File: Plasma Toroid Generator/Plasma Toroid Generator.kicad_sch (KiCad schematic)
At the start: 14 parts, among them J1 Conn_01x02, J2 Conn_01x01, J3 Conn_01x01, J4 Conn_01x01, J5 Conn_01x01, Q1 IRFP260

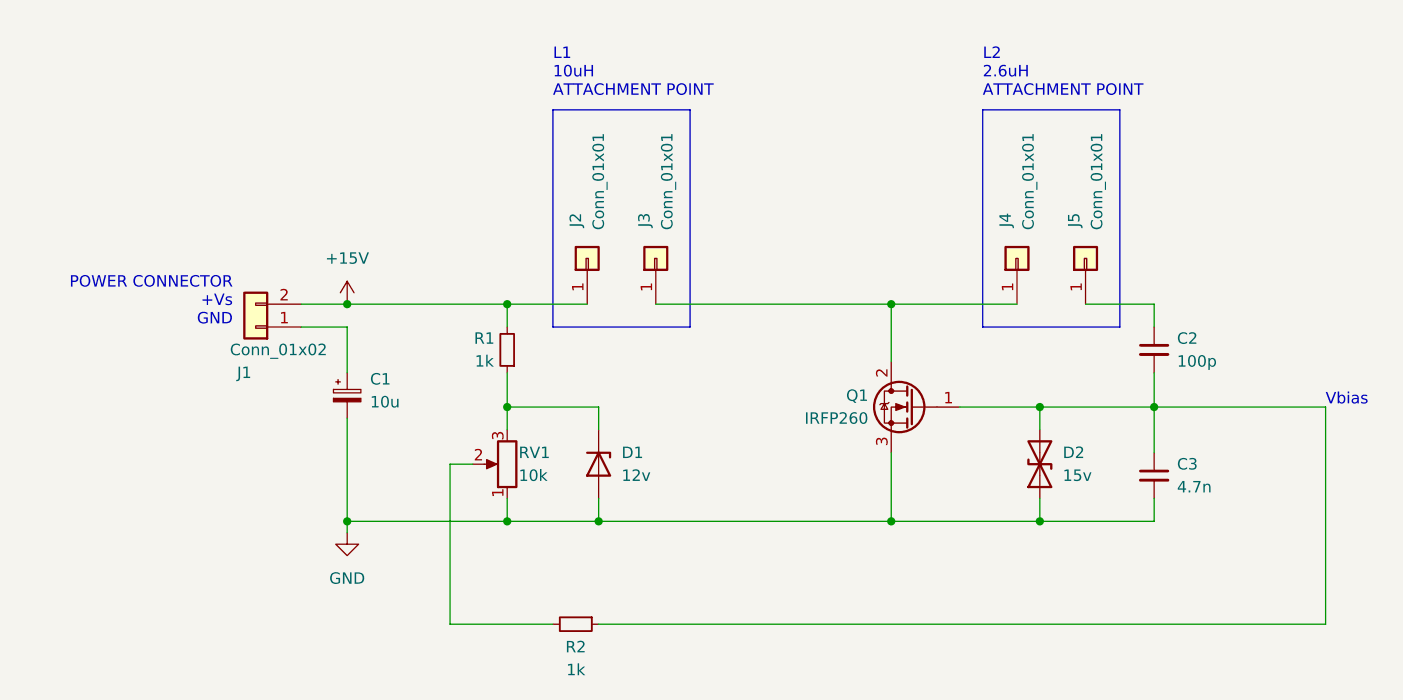
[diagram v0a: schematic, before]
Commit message: Updated PCB layout to fix errors in cap placement
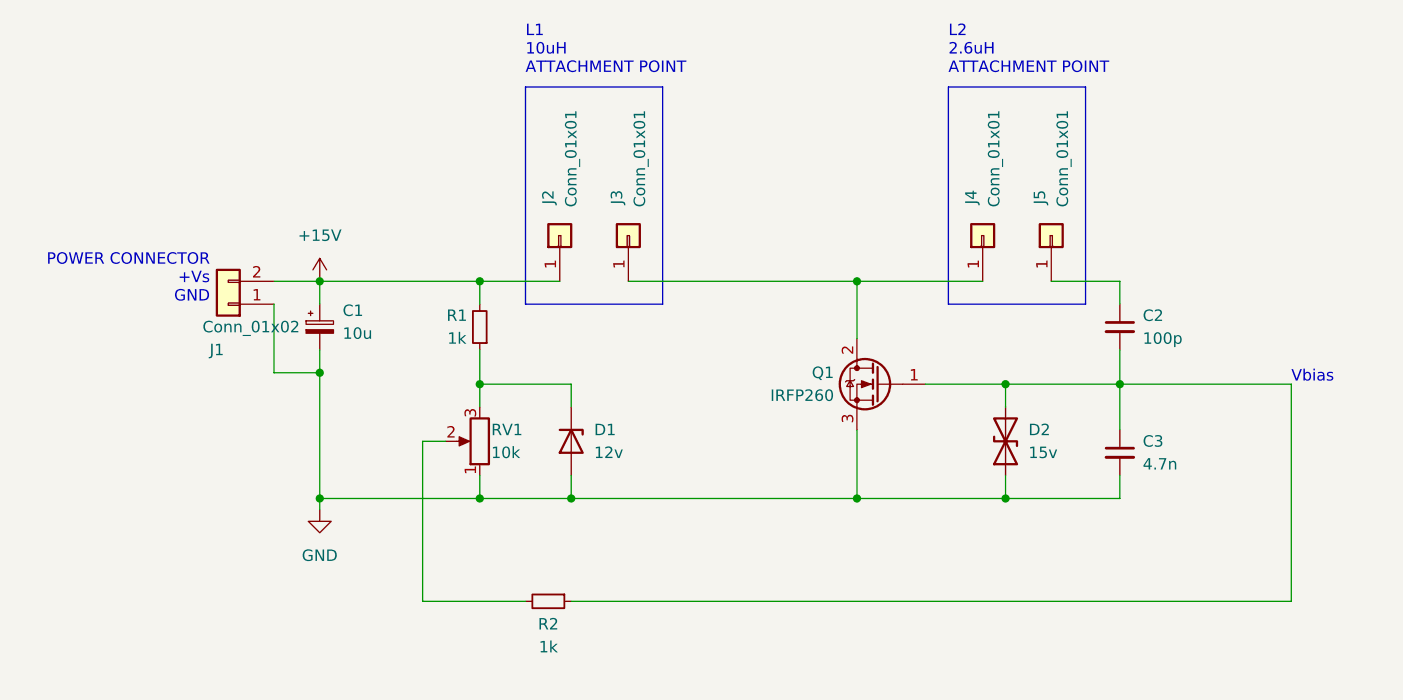
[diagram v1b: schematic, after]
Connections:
- net +15V: now also C1.1
- net GND: now also J1.1 (Pin_1)
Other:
- moved on the sheet: C1, C2, C3, D1, D2, J1, J2, J3, J4, J5, Q1, R1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

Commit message: Updates to model to accurately reflect the physical circuit
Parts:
- J1: footprint TerminalBlock_Phoenix:TerminalBlock_Phoenix_PT-1,5-2-3.5-H_1x02_P3.50mm_Horizontal -> TerminalBlock_Phoenix:TerminalBlock_Phoenix_PT-1,5-2-5.0-H_1x02_P5.00mm_Horizontal
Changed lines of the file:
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@@
     (property "Reference" "J1" (id 0) (at 80.01 91.44 0))
     (property "Value" "Conn_01x02" (id 1) (at 83.82 88.9 0))
-    (property "Footprint" "TerminalBlock_Phoenix:TerminalBlock_Phoenix_PT-1,5-2-3.5-H_1x02_P3.50mm_Horizontal" (id 2) (at 81.28 86.36 0)
+    (property "Footprint" "TerminalBlock_Phoenix:TerminalBlock_Phoenix_PT-1,5-2-5.0-H_1x02_P5.00mm_Horizontal" (id 2) (at 81.28 86.36 0)
       (effects (font (size 1.27 1.27)) hide)
     )
@@
     )
     (path "/179c001d-ac29-4e34-ad76-bad17fa62990"
-      (reference "J1") (unit 1) (value "Conn_01x02") (footprint "TerminalBlock_Phoenix:TerminalBlock_Phoenix_PT-1,5-2-3.5-H_1x02_P3.50mm_Horizontal")
+      (reference "J1") (unit 1) (value "Conn_01x02") (footprint "TerminalBlock_Phoenix:TerminalBlock_Phoenix_PT-1,5-2-5.0-H_1x02_P5.00mm_Horizontal")
     )
     (path "/ef06664d-39b2-4929-8de3-860fd81db3d0"
